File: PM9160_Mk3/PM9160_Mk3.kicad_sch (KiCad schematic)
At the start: 87 parts, among them J1 Conn_Coaxial, U1 BGA2869, U2 ATtiny416-M, U3 SY100EL33L, U4 SY100EL33L, U5 LM317L_TO92

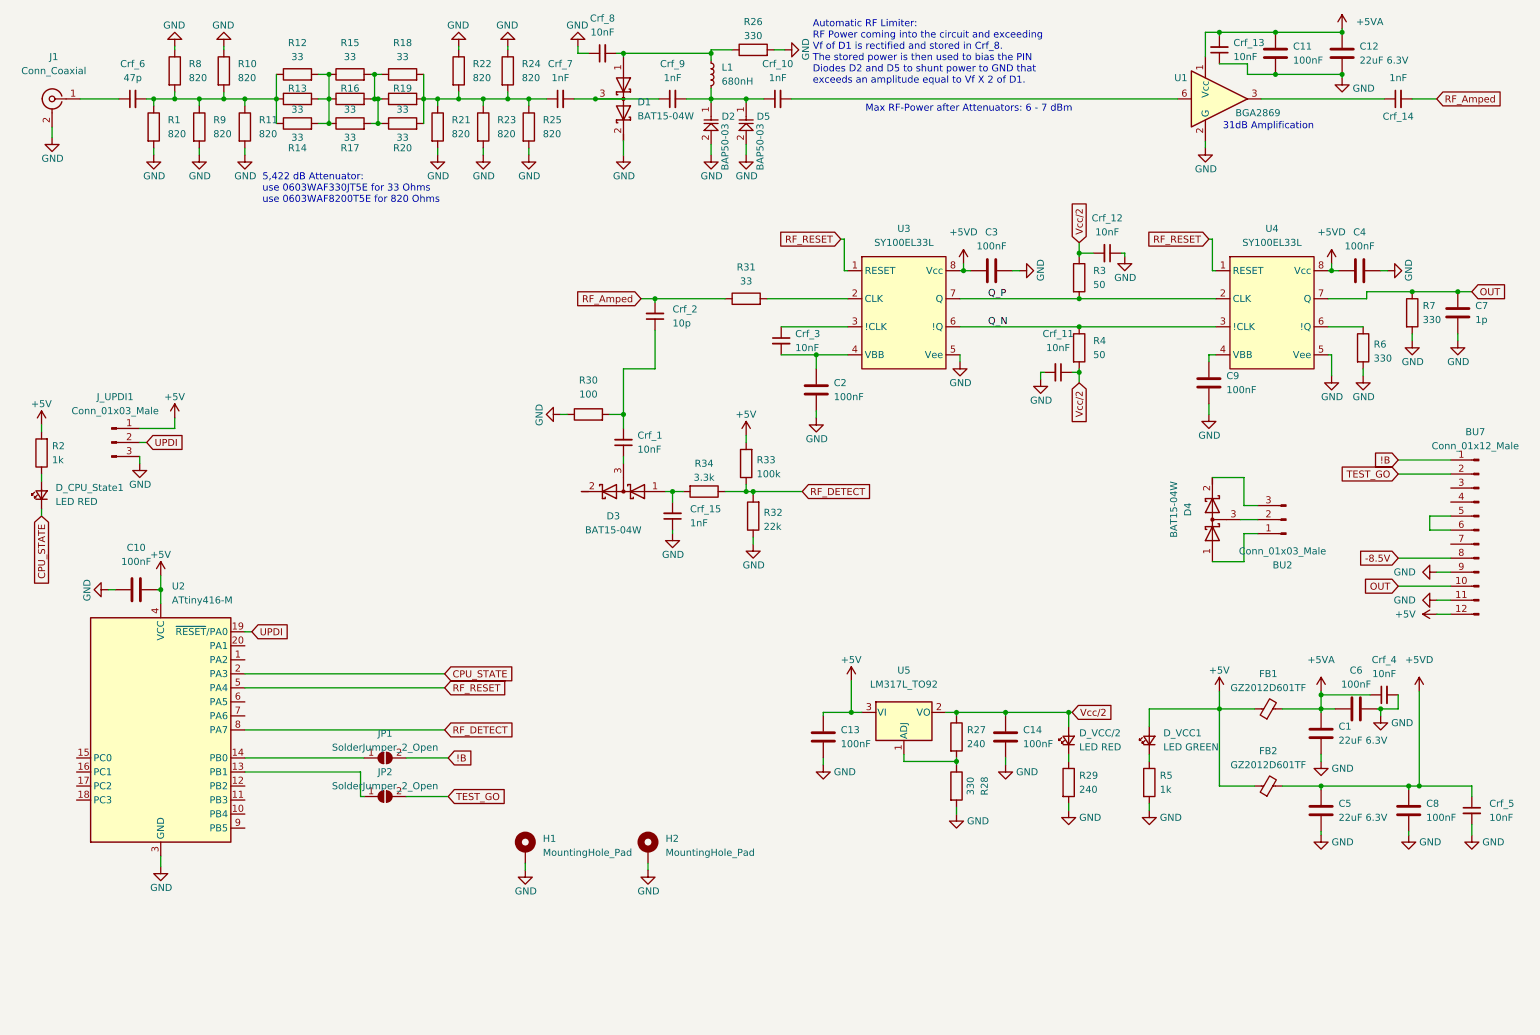
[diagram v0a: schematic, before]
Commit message: Minor Changes to PCB layout, cleaned up schematic, fixed some DRC/ERC errors and warnings, made board compatible with Aislers "simple" PCB Service
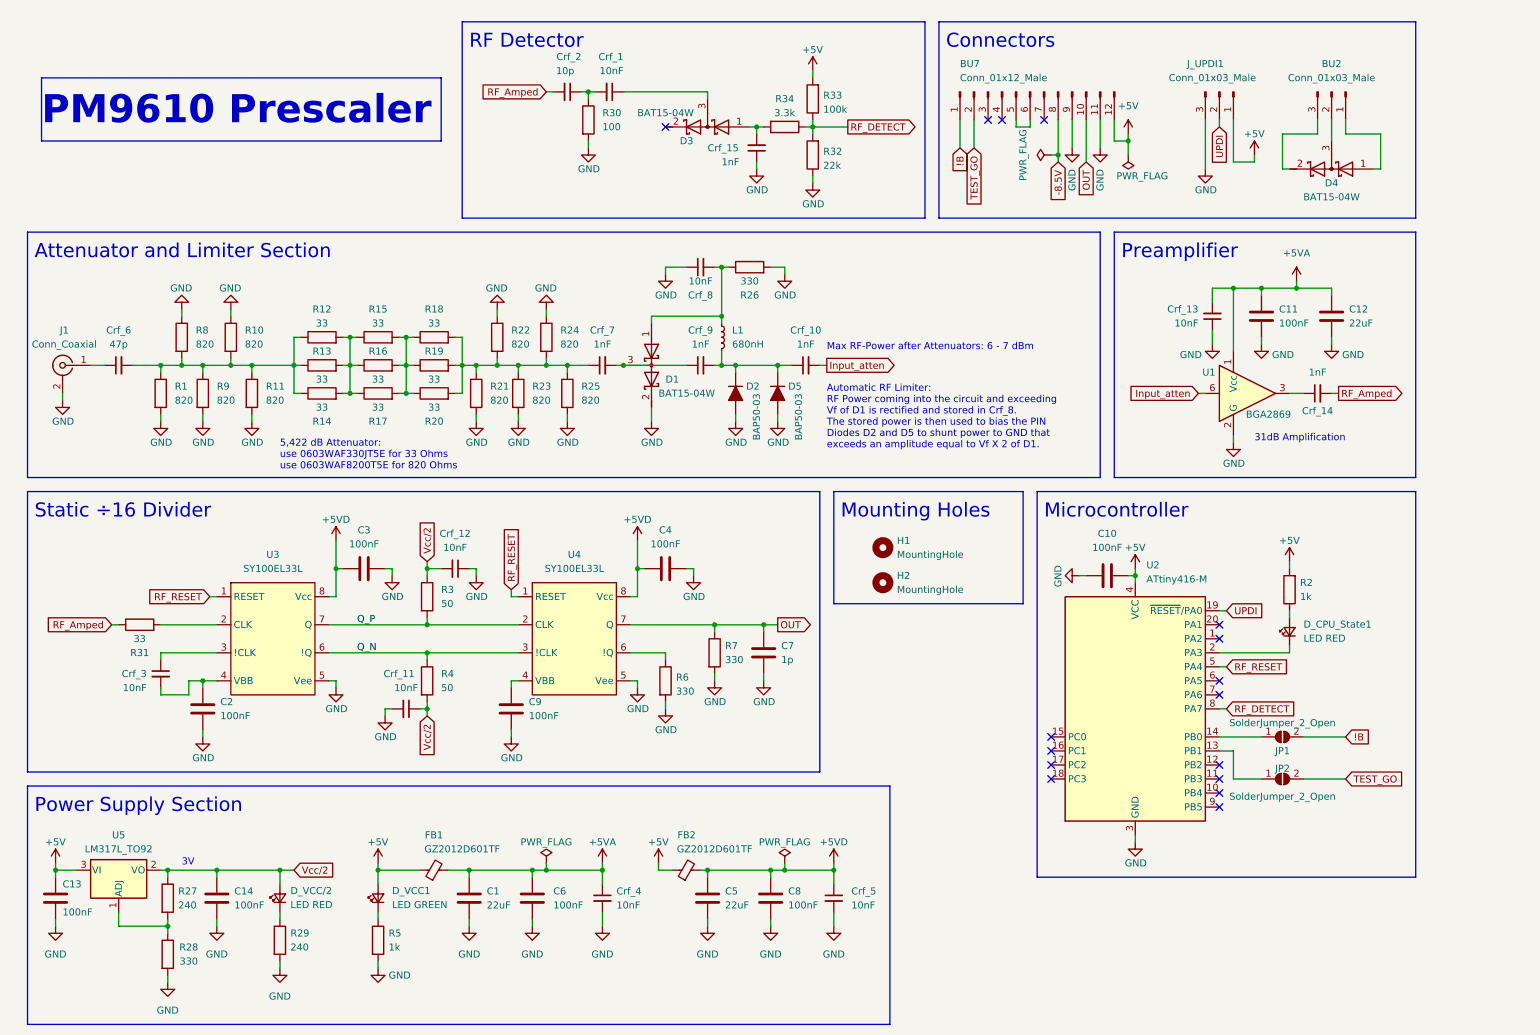
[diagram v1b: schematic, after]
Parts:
- removed H1, H2: MountingHole_Pad, MountingHole:MountingHole_3.2mm_M3_DIN965, symbol Mechanical:MountingHole_Pad
- added H1, H2: MountingHole, MountingHole:MountingHole_3.2mm_M3_DIN965, symbol Mechanical:MountingHole
- BU2, J_UPDI1: symbol Connector:Conn_01x03_Male -> Connector:Conn_01x03_Pin
- BU7: symbol Connector:Conn_01x12_Male -> Connector:Conn_01x12_Pin
- C1, C12, C5: value 22uF 6.3V -> 22uF; WV (none) -> 6.3V
- D2, D5: symbol RF:PIN_Diode -> PCM_Diode_AKL:BAP50-03
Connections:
- net GND: now also R30.2; no longer R30.1
- net at Crf_1.2, Crf_2.1: now also R30.1; no longer R30.2
- net Input_atten: now reaches Crf_10.2, U1.6
- net CPU_STATE: no longer names the net of D_CPU_State1.1 (K), U2.2 (PA3)
- no-connect marks 0 -> 16
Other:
- note added: "3V"
- note added: "Attenuator and Limiter Section"
- note added: "Connectors"
- note added: "Microcontroller"
- note added: "Mounting Holes"
- note added: "PM9610 Prescaler"
- note added: "Power Supply Section"
- note added: "Preamplifier"
- note added: "RF Detector"
- note added: "Static ÷16 Divider"
- moved on the sheet: BU2, BU7, C1, C10, C11, C12, C13, C14, C2, C3, C4, C5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

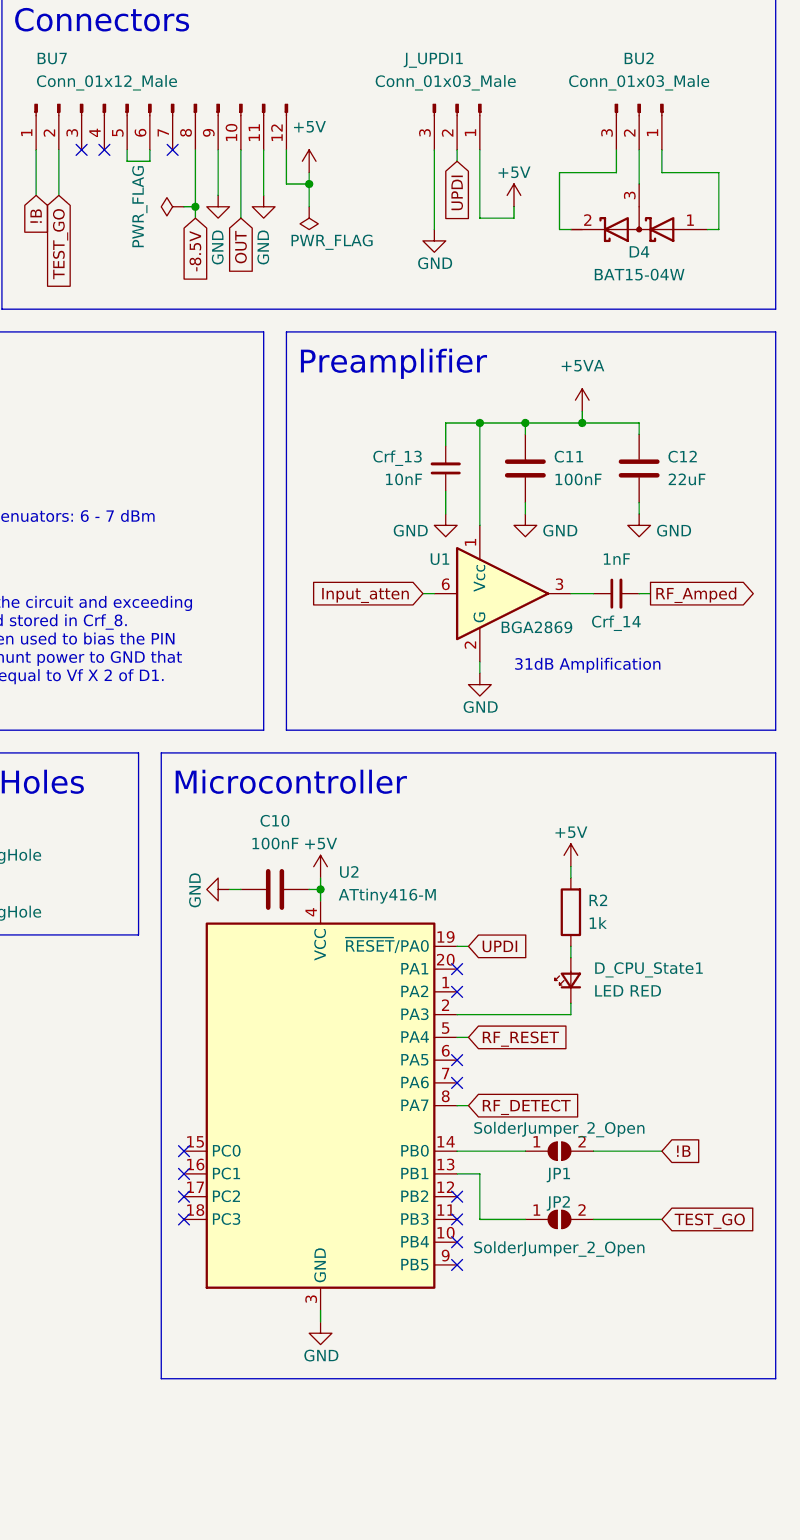
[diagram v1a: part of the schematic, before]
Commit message: changed microcontroller to SOIC-8 Attiny412 for easier handsoldering.
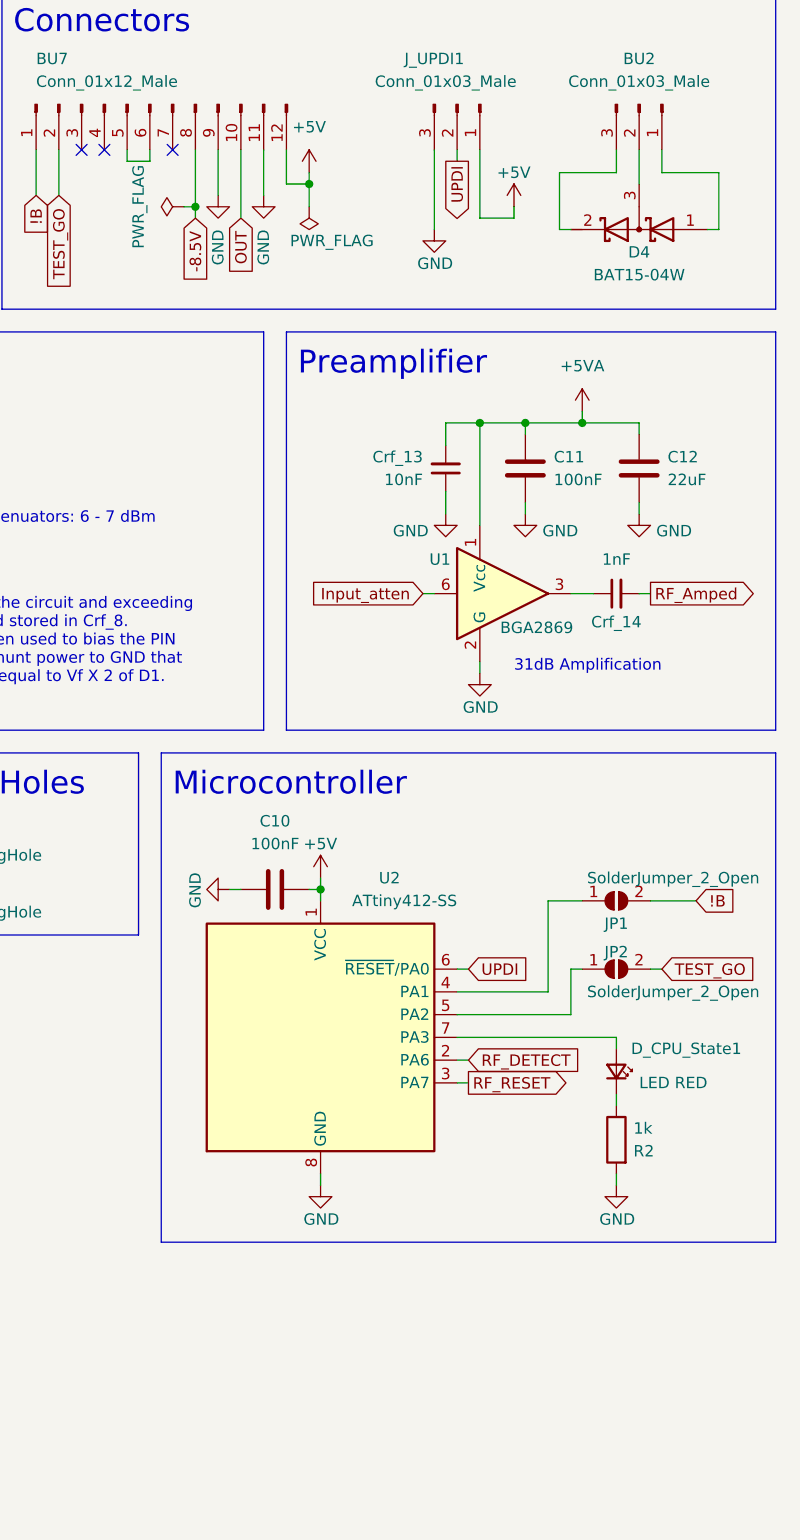
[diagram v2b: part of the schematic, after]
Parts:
- removed U2: ATtiny416-M, Package_DFN_QFN:VQFN-20-1EP_3x3mm_P0.4mm_EP1.7x1.7mm, symbol MCU_Microchip_ATtiny:ATtiny416-M
- added U2: ATtiny412-SS, Package_SO:SOIC-8_3.9x4.9mm_P1.27mm, symbol MCU_Microchip_ATtiny:ATtiny412-SS
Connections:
- net +5V: now also U2.1 (VCC); no longer R2.2
- net GND: now also R2.2, U2.8 (GND)
- net RF_DETECT: now also U2.2 (PA6)
- net RF_RESET: now also U2.3 (PA7)
- net UPDI: now also U2.6 (~{RESET}/PA0)
- net at JP1.1 (A): now also U2.4 (PA1)
- net at JP2.1 (A): now also U2.5 (PA2)
- net at D_CPU_State1.1 (K): now also R2.1
- net at D_CPU_State1.2 (A): now also U2.7 (PA3); no longer R2.1
- no-connect marks 16 -> 4
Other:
- moved on the sheet: D_CPU_State1, R2

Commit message: Changed resistor-footprints of the capacitors to proper capacitor footprints.
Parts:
- C1, C10, C11, C12, C13, C14, C2, C3, C4, C5, C6, C7, C8, C9: footprint Resistor_SMD:R_0603_1608Metric -> Capacitor_SMD:C_0603_1608Metric
- Crf_1, Crf_10, Crf_11, Crf_12, Crf_13, Crf_14, Crf_15, Crf_2, Crf_3, Crf_4, Crf_5, Crf_6, Crf_7, Crf_8, Crf_9: footprint Resistor_SMD:R_0402_1005Metric -> Capacitor_SMD:C_0402_1005Metric
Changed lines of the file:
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@@
       (effects (font (size 1.27 1.27)))
     )
-    (property "Footprint" "Resistor_SMD:R_0402_1005Metric" (at 118.11 76.2 0)
+    (property "Footprint" "Capacitor_SMD:C_0402_1005Metric" (at 118.11 76.2 0)
       (effects (font (size 1.27 1.27)) hide)
     )
@@
       (effects (font (size 1.27 1.27)) (justify left))
     )
-    (property "Footprint" "Resistor_SMD:R_0603_1608Metric" (at 251.1552 71.12 0)
+    (property "Footprint" "Capacitor_SMD:C_0603_1608Metric" (at 251.1552 71.12 0)
       (effects (font (size 1.27 1.27)) hide)
     )
@@
       (effects (font (size 1.27 1.27)))
     )
-    (property "Footprint" "Resistor_SMD:R_0402_1005Metric" (at 30.48 76.2 0)
+    (property "Footprint" "Capacitor_SMD:C_0402_1005Metric" (at 30.48 76.2 0)
       (effects (font (size 1.27 1.27)) hide)
     )
@@
       (effects (font (size 1.27 1.27)) (justify right))
     )
-    (property "Footprint" "Resistor_SMD:R_0402_1005Metric" (at 146.05 36.83 0)
+    (property "Footprint" "Capacitor_SMD:C_0402_1005Metric" (at 146.05 36.83 0)
       (effects (font (size 1.27 1.27)) hide)
     )
@@
       (effects (font (size 1.27 1.27)) (justify right))
     )
-    (property "Footprint" "Resistor_SMD:R_0402_1005Metric" (at 228.6 67.31 0)
+    (property "Footprint" "Capacitor_SMD:C_0402_1005Metric" (at 228.6 67.31 0)
       (effects (font (size 1.27 1.27)) hide)
     )
@@
       (effects (font (size 1.27 1.27)) (justify right))
     )
-    (property "Footprint" "Resistor_SMD:R_0603_1608Metric" (at 236.5248 63.5 0)
+    (property "Footprint" "Capacitor_SMD:C_0603_1608Metric" (at 236.5248 63.5 0)
       (effects (font (size 1.27 1.27)) hide)
     )
@@
       (effects (font (size 1.27 1.27)) (justify left))
     )
-    (property "Footprint" "Resistor_SMD:R_0402_1005Metric" (at 38.1 132.08 0)
+    (property "Footprint" "Capacitor_SMD:C_0402_1005Metric" (at 38.1 132.08 0)
       (effects (font (size 1.27 1.27)) hide)
     )
@@
       (effects (font (size 1.27 1.27)) (justify right))
     )
-    (property "Footprint" "Resistor_SMD:R_0402_1005Metric" (at 111.76 26.67 0)
+    (property "Footprint" "Capacitor_SMD:C_0402_1005Metric" (at 111.76 26.67 0)
       (effects (font (size 1.27 1.27)) hide)
     )
@@
       (effects (font (size 1.27 1.27)) (justify left))
     )
-    (property "Footprint" "Resistor_SMD:R_0402_1005Metric" (at 118.11 172.72 0)
+    (property "Footprint" "Capacitor_SMD:C_0402_1005Metric" (at 118.11 172.72 0)
       (effects (font (size 1.27 1.27)) hide)
     )
@@
       (effects (font (size 1.27 1.27)))
     )
-    (property "Footprint" "Resistor_SMD:R_0603_1608Metric" (at 213.36 113.3348 0)
+    (property "Footprint" "Capacitor_SMD:C_0603_1608Metric" (at 213.36 113.3348 0)
       (effects (font (size 1.27 1.27)) hide)
     )
@@
       (effects (font (size 1.27 1.27)) (justify left))
     )
-    (property "Footprint" "Resistor_SMD:R_0603_1608Metric" (at 46.6852 142.24 0)
+    (property "Footprint" "Capacitor_SMD:C_0603_1608Metric" (at 46.6852 142.24 0)
       (effects (font (size 1.27 1.27)) hide)
     )
@@
       (effects (font (size 1.27 1.27)) (justify left))
     )
-    (property "Footprint" "Resistor_SMD:R_0603_1608Metric" (at 94.9452 176.53 0)
+    (property "Footprint" "Capacitor_SMD:C_0603_1608Metric" (at 94.9452 176.53 0)
       (effects (font (size 1.27 1.27)) hide)
     )
@@
       (effects (font (size 1.27 1.27)) (justify left))
     )
-    (property "Footprint" "Resistor_SMD:R_0603_1608Metric" (at 20.0152 176.53 0)
+    (property "Footprint" "Capacitor_SMD:C_0603_1608Metric" (at 20.0152 176.53 0)
       (effects (font (size 1.27 1.27)) hide)
     )
@@
       (effects (font (size 1.27 1.27)) (justify left))
     )
-    (property "Footprint" "Resistor_SMD:R_0402_1005Metric" (at 160.02 172.72 0)
+    (property "Footprint" "Capacitor_SMD:C_0402_1005Metric" (at 160.02 172.72 0)
       (effects (font (size 1.27 1.27)) hide)
     )
@@
       (effects (font (size 1.27 1.27)) (justify left))
     )
-    (property "Footprint" "Resistor_SMD:R_0603_1608Metric" (at 148.2852 132.08 0)
+    (property "Footprint" "Capacitor_SMD:C_0603_1608Metric" (at 148.2852 132.08 0)
       (effects (font (size 1.27 1.27)) hide)
     )
@@
       (effects (font (size 1.27 1.27)))
     )
-    (property "Footprint" "Resistor_SMD:R_0402_1005Metric" (at 247.65 81.28 0)
+    (property "Footprint" "Capacitor_SMD:C_0402_1005Metric" (at 247.65 81.28 0)
       (effects (font (size 1.27 1.27)) hide)
     )
@@
       (effects (font (size 1.27 1.27)) (justify right))
     )
-    (property "Footprint" "Resistor_SMD:R_0402_1005Metric" (at 119.38 26.67 0)
+    (property "Footprint" "Capacitor_SMD:C_0402_1005Metric" (at 119.38 26.67 0)
       (effects (font (size 1.27 1.27)) hide)
     )
@@
       (effects (font (size 1.27 1.27)))
     )
-    (property "Footprint" "Resistor_SMD:R_0603_1608Metric" (at 133.35 112.0648 0)
+    (property "Footprint" "Capacitor_SMD:C_0603_1608Metric" (at 133.35 112.0648 0)
       (effects (font (size 1.27 1.27)) hide)
     )
@@
       (effects (font (size 1.27 1.27)))
     )
-    (property "Footprint" "Resistor_SMD:R_0402_1005Metric" (at 82.55 138.43 0)
+    (property "Footprint" "Capacitor_SMD:C_0402_1005Metric" (at 82.55 138.43 0)
       (effects (font (size 1.27 1.27)) hide)
     )
@@
       (effects (font (size 1.27 1.27)) (justify left))
     )
-    (property "Footprint" "Resistor_SMD:R_0603_1608Metric" (at 49.2252 176.53 0)
+    (property "Footprint" "Capacitor_SMD:C_0603_1608Metric" (at 49.2252 176.53 0)
       (effects (font (size 1.27 1.27)) hide)
     )
@@
       (effects (font (size 1.27 1.27)))
     )
-    (property "Footprint" "Resistor_SMD:R_0402_1005Metric" (at 135.89 58.42 0)
+    (property "Footprint" "Capacitor_SMD:C_0402_1005Metric" (at 135.89 58.42 0)
       (effects (font (size 1.27 1.27)) hide)
     )
@@
       (effects (font (size 1.27 1.27)) (justify left))
     )
-    (property "Footprint" "Resistor_SMD:R_0603_1608Metric" (at 149.5552 176.53 0)
+    (property "Footprint" "Capacitor_SMD:C_0603_1608Metric" (at 149.5552 176.53 0)
       (effects (font (size 1.27 1.27)) hide)
     )
@@
       (effects (font (size 1.27 1.27)) (justify left))
     )
-    (property "Footprint" "Resistor_SMD:R_0603_1608Metric" (at 138.1252 176.53 0)
+    (property "Footprint" "Capacitor_SMD:C_0603_1608Metric" (at 138.1252 176.53 0)
       (effects (font (size 1.27 1.27)) hide)
     )
@@
       (effects (font (size 1.27 1.27)))
     )
-    (property "Footprint" "Resistor_SMD:R_0603_1608Metric" (at 78.74 112.0648 0)
+    (property "Footprint" "Capacitor_SMD:C_0603_1608Metric" (at 78.74 112.0648 0)
       (effects (font (size 1.27 1.27)) hide)
     )
@@
       (effects (font (size 1.27 1.27)))
     )
-    (property "Footprint" "Resistor_SMD:R_0402_1005Metric" (at 154.94 76.2 0)
+    (property "Footprint" "Capacitor_SMD:C_0402_1005Metric" (at 154.94 76.2 0)
       (effects (font (size 1.27 1.27)) hide)
     )
@@
       (effects (font (size 1.27 1.27)) (justify left))
     )
-    (property "Footprint" "Resistor_SMD:R_0603_1608Metric" (at 106.3752 176.53 0)
+    (property "Footprint" "Capacitor_SMD:C_0603_1608Metric" (at 106.3752 176.53 0)
       (effects (font (size 1.27 1.27)) hide)
     )
@@
       (effects (font (size 1.27 1.27)) (justify left))
     )
-    (property "Footprint" "Resistor_SMD:R_0603_1608Metric" (at 102.5652 142.24 0)
+    (property "Footprint" "Capacitor_SMD:C_0603_1608Metric" (at 102.5652 142.24 0)
       (effects (font (size 1.27 1.27)) hide)
     )
@@
       (effects (font (size 1.27 1.27)))
     )
-    (property "Footprint" "Resistor_SMD:R_0402_1005Metric" (at 135.89 76.2 0)
+    (property "Footprint" "Capacitor_SMD:C_0402_1005Metric" (at 135.89 76.2 0)
       (effects (font (size 1.27 1.27)) hide)
     )
@@
       (effects (font (size 1.27 1.27)))
     )
-    (property "Footprint" "Resistor_SMD:R_0402_1005Metric" (at 91.44 113.03 0)
+    (property "Footprint" "Capacitor_SMD:C_0402_1005Metric" (at 91.44 113.03 0)
       (effects (font (size 1.27 1.27)) hide)
     )
